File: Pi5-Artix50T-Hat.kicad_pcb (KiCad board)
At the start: 4 copper layers, 65 x 56 mm, 155 parts, among them J1 GPIO, J2 Molex 0878321420, J3 68711614522, J4 Molex 0878321420, U1 FT24C256A, U10 AP62200TWU-7, U11 AP62200TWU-7, U12 AP62200TWU-7, U2 XC7A50T-FGG484, U9 AP62200TWU-7, X1 50MHz

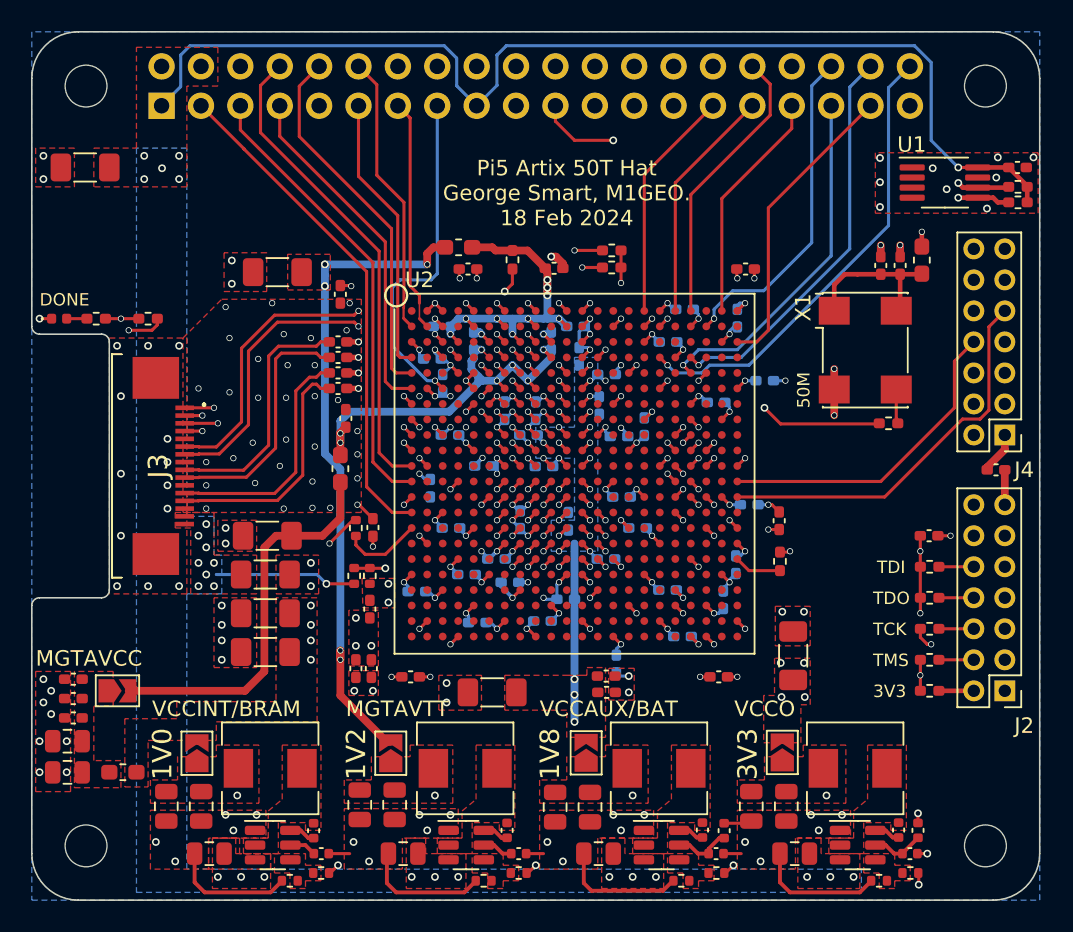
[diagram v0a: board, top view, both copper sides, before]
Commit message: Ordered boards from JLCPCB for V1
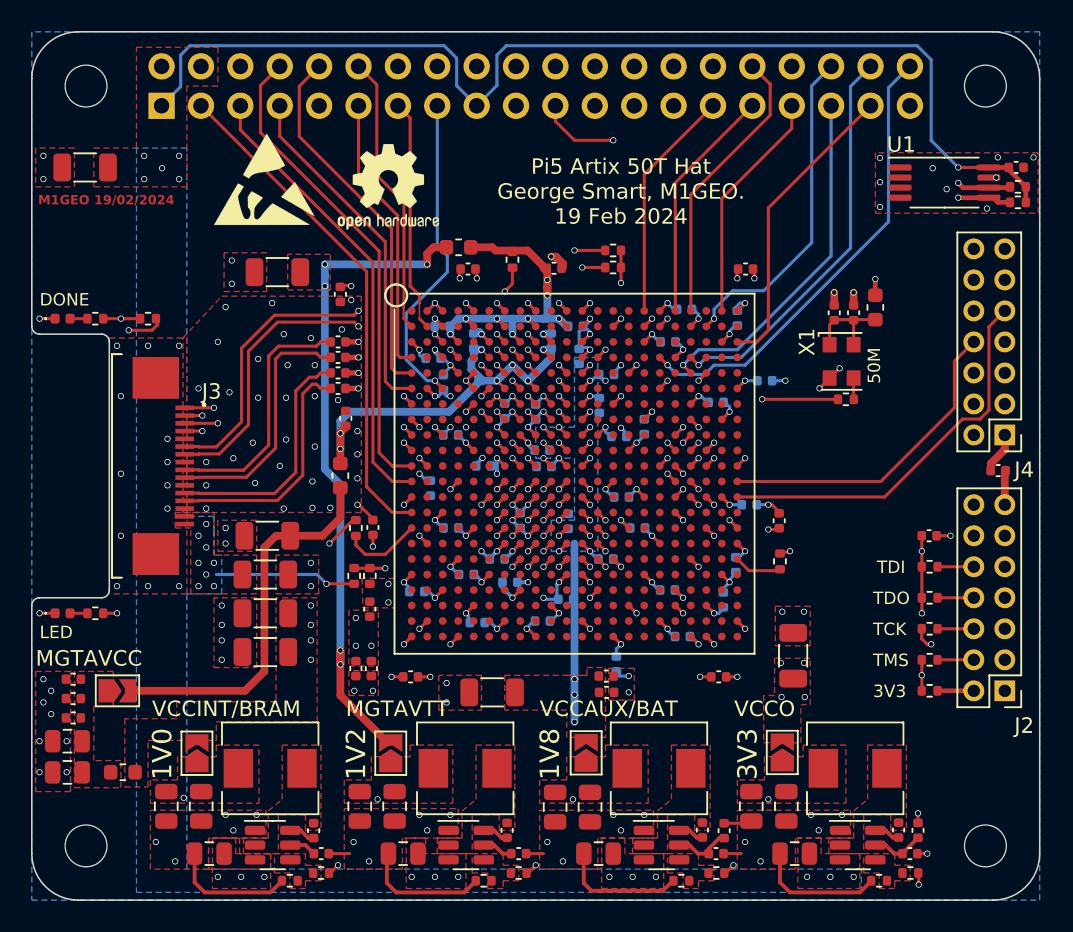
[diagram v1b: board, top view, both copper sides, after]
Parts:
- added D2: RED, LED_SMD:LED_0402_1005Metric, F.Cu at (102.0, 81.5)
- added R18: 1k, Resistor_SMD:R_0402_1005Metric, F.Cu at (104.1, 81.5)
- added REF**: ESD-Logo_6.6x6mm_SilkScreen, Symbol:ESD-Logo_6.6x6mm_SilkScreen, F.Cu at (115.0, 53.5)
- added REF**: OSHW-Logo2_7.3x6mm_SilkScreen, Symbol:OSHW-Logo2_7.3x6mm_SilkScreen, F.Cu at (123.0, 54.0)
- C1, C10, C107, C11, C112, C113, C12, C13, C15, C19, C2, C21, C22, C25, C26, C27, C28, C29, C3, C30, C31, C32, C33, C34, C35, C36, C38, C39, C4, C40, C41, C42, C43, C44, C45, C46, C47, C48, C49, C5, C50, C51, C53, C54, C55, C56, C57, C58, C59, C6, C61, C62, C63, C64, C65, C66, C67, C68, C69, C7, C70, C72, C73, C74, C75, C76, C93, C94: footprint Capacitor_SMD:C_0402_1005Metric_Pad0.74x0.62mm_HandSolder -> Capacitor_SMD:C_0402_1005Metric
- C23, C24, C37, C77, C78, C79, C8, C96: footprint Capacitor_SMD:C_1206_3216Metric_Pad1.33x1.80mm_HandSolder -> Capacitor_SMD:C_1206_3216Metric
- FB1, FB2, FB3, FB4: footprint Inductor_SMD:L_0603_1608Metric_Pad1.05x0.95mm_HandSolder -> Inductor_SMD:L_0603_1608Metric
- JP10, JP11, JP12, JP8, JP9: value ID_WP -> JUMPER
- R1, R2, R3, R5, R6, R7, R8, R9: value 3.9k -> 3.2k; footprint Resistor_SMD:R_0402_1005Metric_Pad0.72x0.64mm_HandSolder -> Resistor_SMD:R_0402_1005Metric
- R10, R11, R12, R13, R16, R4: footprint Resistor_SMD:R_0402_1005Metric_Pad0.72x0.64mm_HandSolder -> Resistor_SMD:R_0402_1005Metric
- R17: value 3.9k -> 3.2k
- U1: value FT24C256A -> BL24C256A; footprint Package_SO:MSOP-8_3x3mm_P0.65mm -> Package_SO:TSSOP-8_4.4x3mm_P0.65mm
- X1: footprint Oscillator:Oscillator_SMD_Abracon_ASV-4Pin_7.0x5.1mm -> Oscillator:Oscillator_SMD_EuroQuartz_XO32-4Pin_3.2x2.5mm
- moved C93 4.28 mm to (151.8, 62.1)
- moved C94 4.28 mm to (153.0, 62.1)
- moved FB3 4.28 mm to (154.4, 61.8)
- moved R16 3.16 mm to (152.5, 67.7)
- moved X1 1.69 mm to (152.2, 65.3), turned to 0 degrees
- moved C42 1.31 mm to (132.9, 71.0)
- moved FB1 0.45 mm to (119.9, 72.6)
- moved D1 0.22 mm to (102.0, 62.5)
- moved C22 0.15 mm to (162.3, 72.3)
- moved C115 0.10 mm to (123.4, 94.0)
- moved C119 0.10 mm to (121.2, 94.0)
- moved R8 0.09 mm to (137.5, 59.2), turned to 0 degrees
- moved C1 0.09 mm to (163.5, 52.8)
- moved R9 0.09 mm to (137.5, 58.1), turned to 0 degrees
- moved C34 0.09 mm to (132.5, 68.5)
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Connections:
- R1 pad 1: +3.3VP -> /Raspberry Pi 5/ID_SDA
- R1 pad 2: /Raspberry Pi 5/ID_SDA -> +3.3VP
- R17 pad 1: Net-(U2C-IO_L20P_T3_35) -> /FPGA Top/PCIE_PWR_EN
- R17 pad 2: /FPGA Top/PCIE_PWR_EN -> Net-(U2C-IO_L20P_T3_35)
- R2 pad 1: +3.3VP -> /Raspberry Pi 5/ID_SCL
- R2 pad 2: /Raspberry Pi 5/ID_SCL -> +3.3VP
- R3 pad 1: +3V3 -> TMS
- R3 pad 2: TMS -> +3V3
- R5 pad 1: +3V3 -> TDO
- R5 pad 2: TDO -> +3V3
- R6 pad 1: +3V3 -> TDI
- R6 pad 2: TDI -> +3V3
- R7 pad 1: TCK -> GND
- R7 pad 2: GND -> TCK
- R8 pad 1: +3V3 -> /Raspberry Pi 5/GPIO25
- R8 pad 2: /Raspberry Pi 5/GPIO25 -> +3V3
- R9 pad 1: +3V3 -> /Raspberry Pi 5/GPIO24
- R9 pad 2: /Raspberry Pi 5/GPIO24 -> +3V3
- U2 pad AB1: unconnected-(U2C-IO_L7N_T1_34-PadAB1) -> /FPGA Top/FPGA_LED
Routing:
- net /FPGA Top/FPGA_LED: track 0.00 -> 24.3 mm, vias 0 -> 2
- net Net-(JP11-A): track 9.76 -> 17.1 mm
- net Net-(JP10-A): track 9.76 -> 17.1 mm
- net Net-(JP9-A): track 9.75 -> 16.9 mm
- net Net-(JP12-A): track 9.70 -> 16.0 mm
- net Net-(X1-EN): track 10.1 -> 5.95 mm
- net /FPGA Top/CLK50MHZ: track 15.4 -> 12.3 mm
- net /Raspberry Pi 5/GPIO22: track 22.2 -> 20.9 mm
- net Net-(D2-A): track 0.00 -> 1.03 mm
- net /FPGA Top/PCIE_PWR_EN: track 18.7 -> 17.9 mm
- net Net-(X1-OUT): track 2.00 -> 1.35 mm
- net +1V2_MGTAVTT: track 42.5 -> 43.1 mm
- net /FPGA Top/FPGA Bank 216 (MGT)/MGTAVTT: vias 9 -> 8
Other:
- board text added: "19 Feb 2024 - Pi5 Artix 50T Hat"
- board text added: "JLCJLCJLC"
- board text added: "LED"
- board text added: "M1GEO 19/02/2024"
- board text added: "Pi5 Artix 50T Hat George Smart, M1GEO. 19 Feb 2024"
- board text removed: "18 Feb 2024 - Pi5 Artix 50T Hat"
- board text removed: "Pi5 Artix 50T Hat George Smart, M1GEO. 18 Feb 2024"
